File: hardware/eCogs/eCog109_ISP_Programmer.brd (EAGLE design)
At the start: 47.5 x 28 mm, 3 parts

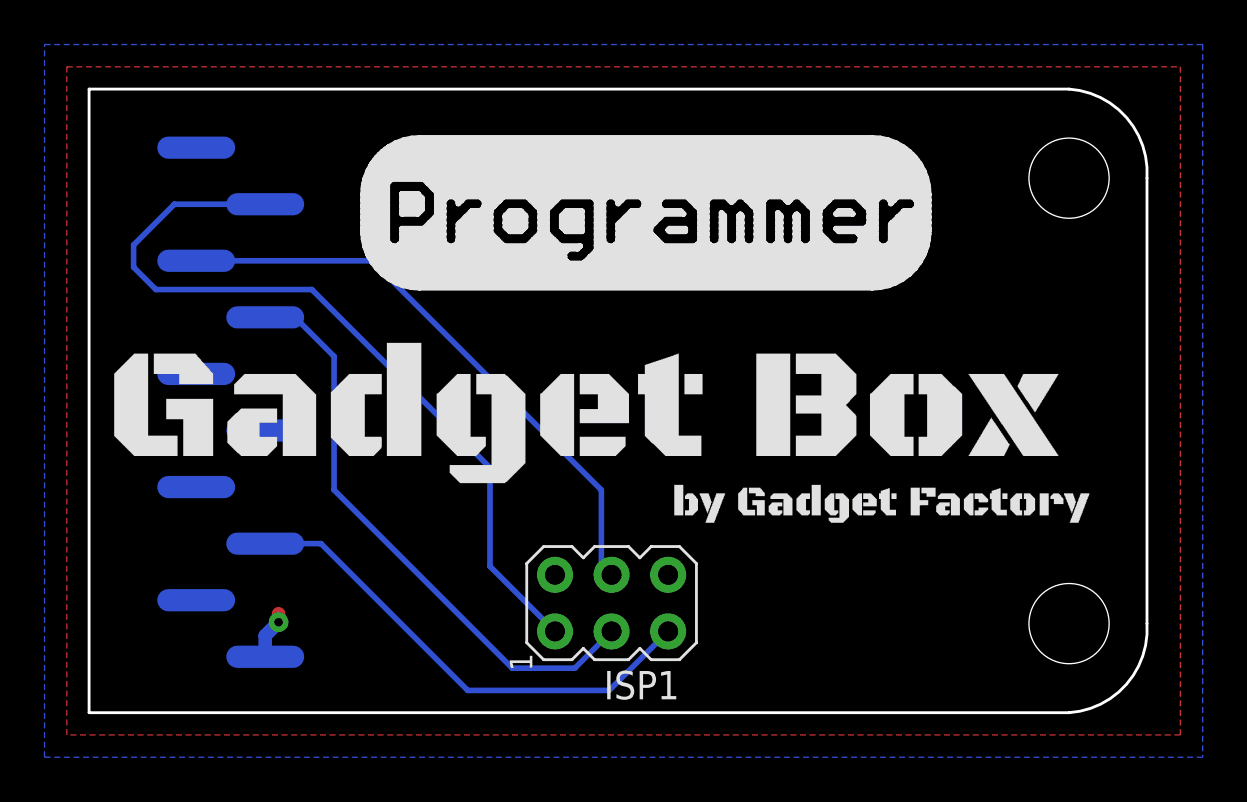
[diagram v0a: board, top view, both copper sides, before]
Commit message: Update eCogs to through hole
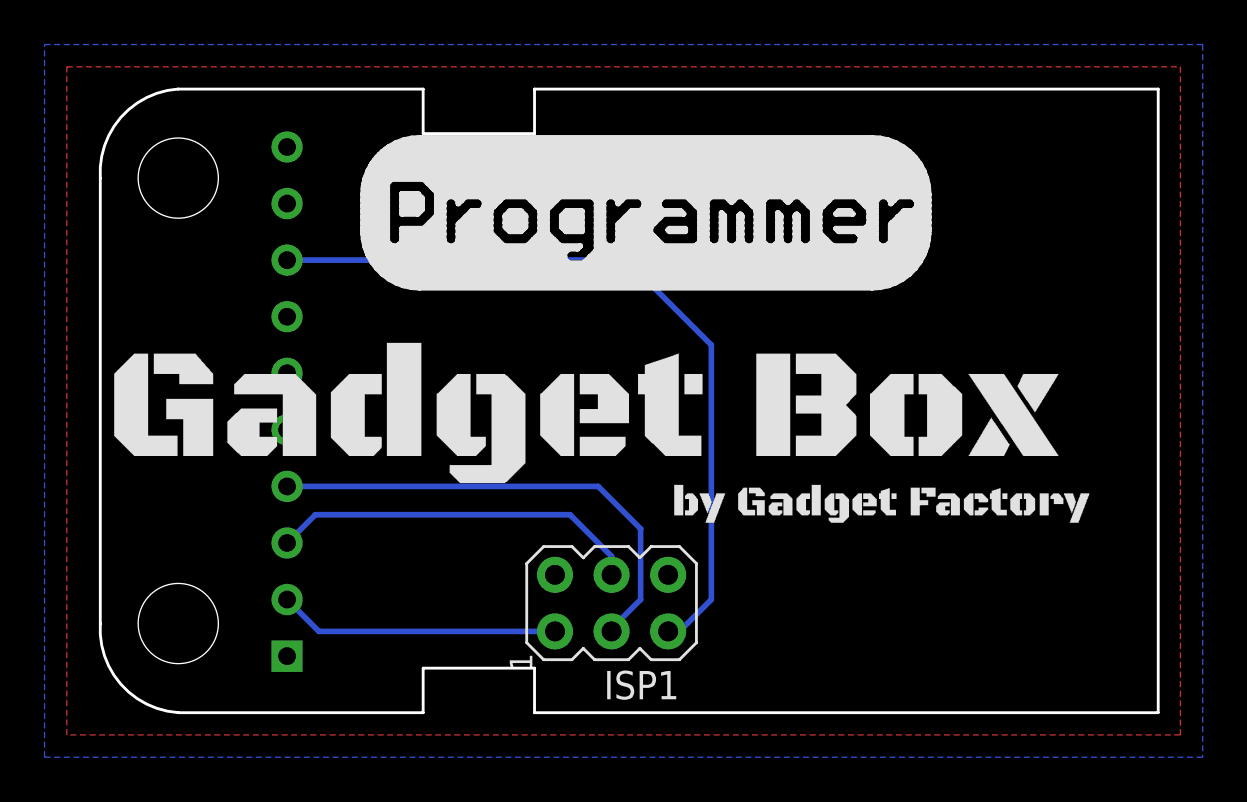
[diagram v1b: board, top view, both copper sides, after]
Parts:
- ECOG: value ECOG_BUSES_ROWECOG_BUSES_SMD -> ECOG_BUSES_ROWTHROUGHHOLE; device eCogs:ECOG_BUSES_SMD -> eCogs:ECOG_BUSES_TH
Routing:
- net N$1: track 36.0 -> 12.6 mm
- net N$3: track 21.9 -> 34.6 mm
- net N$4: track 26.5 -> 16.7 mm
- net N$2: track 26.3 -> 21.8 mm
- net 3V3: track 2.18 -> 0.00 mm, vias 1 -> 0
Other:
- outline, holes or cut-outs redrawn
- board text added: "ecog109 v2.1"
- board text removed: "ecog109 v1.0"
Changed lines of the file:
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@@
 <setting verticaltext="up"/>
 </settings>
-<grid distance="1" unitdist="mm" unit="mm" style="lines" multiple="1" display="yes" altdistance="0.1" altunitdist="mm" altunit="mm"/>
+<grid distance="0.05" unitdist="inch" unit="inch" style="lines" multiple="1" display="yes" altdistance="0.005" altunitdist="inch" altunit="inch"/>
 <layers>
 <layer number="1" name="Top" color="4" fill="1" visible="yes" active="yes"/>
@@
 <layer number="19" name="Unrouted" color="6" fill="1" visible="yes" active="yes"/>
 <layer number="20" name="Dimension" color="15" fill="1" visible="yes" active="yes"/>
-<layer number="21" name="tPlace" color="16" fill="1" visible="yes" active="yes"/>
+<layer number="21" name="tPlace" color="16" fill="1" visible="no" active="yes"/>
 <layer number="22" name="bPlace" color="14" fill="1" visible="yes" active="yes"/>
 <layer number="23" name="tOrigins" color="15" fill="1" visible="yes" active="yes"/>
@@
 <plain>
 <text x="37.559" y="18.415" size="0.8128" layer="22" font="vector" rot="MR0">ecog109.GadgetFactory.net</text>
-<text x="40.702" y="2.159" size="1.016" layer="22" font="vector" rot="MR0">ecog109 v1.0</text>
+<text x="40.702" y="2.159" size="1.016" layer="22" font="vector" rot="MR0">ecog109 v2.1</text>
 <text x="40.702" y="3.429" size="1.016" layer="22" font="vector" rot="MR0">ISP Programmer</text>
 <text x="40.702" y="4.699" size="1.016" layer="22" font="vector" rot="MR0">eCogs</text>
@@
 </autorouter>
 <elements>
-<element name="ECOG" library="eCogs" package="ECOG_BUSES_SMD" value="ECOG_BUSES_ROWECOG_BUSES_SMD" x="0" y="0" smashed="yes">
-<attribute name="DIGIKEY" value="S1013EC-10-ND" x="0" y="0" size="1.778" layer="27" display="off"/>
-</element>
+<element name="ECOG" library="eCogs" package="ECOG_BUSES_TH" value="ECOG_BUSES_ROWTHROUGHHOLE" x="0" y="0" smashed="yes"/>
 <element name="U$1" library="GadgetFactory" package="GADGETBOX_TEXT" value="" x="22.4" y="13.24"/>
 <element name="ISP1" library="adafruit" package="AVRISP" value="AVRISP-6" x="23.46" y="4.92" rot="R90"/>
@@
 </polygon>
 <contactref element="ECOG" pad="3V3"/>
-<wire x1="7.9094" y1="2.51" x2="7.9094" y2="3.4644" width="0.6096" layer="16"/>
-<wire x1="7.9094" y1="3.4644" x2="8.509" y2="4.064" width="0.6096" layer="16"/>
-<via x="8.509" y="4.064" extent="1-16" drill="0.381"/>
-<wire x1="8.509" y1="4.064" x2="8.509" y2="4.445" width="0.6096" layer="1"/>
 <contactref element="ISP1" pad="2"/>
 </signal>
@@
 <contactref element="ECOG" pad="SPI-MISO"/>
 <contactref element="ISP1" pad="1"/>
-<wire x1="7.9094" y1="22.83" x2="3.83" y2="22.83" width="0.254" layer="16"/>
-<wire x1="3.83" y1="22.83" x2="2" y2="21" width="0.254" layer="16"/>
-<wire x1="2" y1="21" x2="2" y2="20" width="0.254" layer="16"/>
-<wire x1="2" y1="20" x2="3" y2="19" width="0.254" layer="16"/>
-<wire x1="3" y1="19" x2="10" y2="19" width="0.254" layer="16"/>
-<wire x1="10" y1="19" x2="18" y2="11" width="0.254" layer="16"/>
-<wire x1="18" y1="11" x2="18" y2="6.57" width="0.254" layer="16"/>
-<wire x1="18" y1="6.57" x2="20.92" y2="3.65" width="0.254" layer="16"/>
+<wire x1="20.92" y1="3.65" x2="10.32" y2="3.65" width="0.254" layer="16"/>
+<wire x1="10.32" y1="3.65" x2="8.89" y2="5.08" width="0.254" layer="16"/>
 </signal>
 <signal name="N$2">
 <contactref element="ECOG" pad="SPI-SCK"/>
 <contactref element="ISP1" pad="3"/>
-<wire x1="7.9094" y1="17.75" x2="9.25" y2="17.75" width="0.254" layer="16"/>
-<wire x1="9.25" y1="17.75" x2="11" y2="16" width="0.254" layer="16"/>
-<wire x1="11" y1="16" x2="11" y2="10" width="0.254" layer="16"/>
-<wire x1="11" y1="10" x2="19" y2="2" width="0.254" layer="16"/>
-<wire x1="19" y1="2" x2="21.81" y2="2" width="0.254" layer="16"/>
-<wire x1="21.81" y1="2" x2="23.46" y2="3.65" width="0.254" layer="16"/>
+<wire x1="23.46" y1="3.65" x2="23.46" y2="3.775" width="0.254" layer="16"/>
+<wire x1="23.46" y1="3.775" x2="24.765" y2="5.08" width="0.254" layer="16"/>
+<wire x1="24.765" y1="5.08" x2="24.765" y2="8.255" width="0.254" layer="16"/>
+<wire x1="24.765" y1="8.255" x2="22.86" y2="10.16" width="0.254" layer="16"/>
+<wire x1="22.86" y1="10.16" x2="8.89" y2="10.16" width="0.254" layer="16"/>
 </signal>
 <signal name="N$3">
 <contactref element="ECOG" pad="RESET"/>
 <contactref element="ISP1" pad="5"/>
-<wire x1="7.9094" y1="7.59" x2="10.41" y2="7.59" width="0.254" layer="16"/>
-<wire x1="10.41" y1="7.59" x2="17" y2="1" width="0.254" layer="16"/>
-<wire x1="17" y1="1" x2="23.35" y2="1" width="0.254" layer="16"/>
-<wire x1="23.35" y1="1" x2="26" y2="3.65" width="0.254" layer="16"/>
+<wire x1="26" y1="3.65" x2="26.51" y2="3.65" width="0.254" layer="16"/>
+<wire x1="26.51" y1="3.65" x2="27.94" y2="5.08" width="0.254" layer="16"/>
+<wire x1="27.94" y1="5.08" x2="27.94" y2="16.51" width="0.254" layer="16"/>
+<wire x1="27.94" y1="16.51" x2="24.13" y2="20.32" width="0.254" layer="16"/>
+<wire x1="24.13" y1="20.32" x2="8.89" y2="20.32" width="0.254" layer="16"/>
 </signal>
 <signal name="N$4">
 <contactref element="ECOG" pad="SPI-MOSI"/>
 <contactref element="ISP1" pad="4"/>
-<wire x1="4.8106" y1="20.29" x2="12.71" y2="20.29" width="0.254" layer="16"/>
-<wire x1="12.71" y1="20.29" x2="23" y2="10" width="0.254" layer="16"/>
-<wire x1="23" y1="10" x2="23" y2="6.65" width="0.254" layer="16"/>
-<wire x1="23" y1="6.65" x2="23.46" y2="6.19" width="0.254" layer="16"/>
+<wire x1="23.46" y1="6.19" x2="23.46" y2="7.02" width="0.254" layer="16"/>
+<wire x1="23.46" y1="7.02" x2="21.59" y2="8.89" width="0.254" layer="16"/>
+<wire x1="21.59" y1="8.89" x2="10.16" y2="8.89" width="0.254" layer="16"/>
+<wire x1="10.16" y1="8.89" x2="8.89" y2="7.62" width="0.254" layer="16"/>
 </signal>
 </signals>
